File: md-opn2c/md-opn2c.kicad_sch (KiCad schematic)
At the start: 51 parts, among them U1 TL072, U3 74HCT08, U4 YM3438

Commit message: Board rev after testing initial prototype
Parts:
- removed JOUT1, JS1, JS2: Conn_01x04_Pin, Connector_JST:JST_EH_B4B-EH-A_1x04_P2.50mm_Vertical, symbol Connector:Conn_01x04_Pin
- removed JPSG1: Conn_01x02_Pin, Connector_JST:JST_EH_B2B-EH-A_1x02_P2.50mm_Vertical, symbol Connector:Conn_01x02_Pin
- removed TP_FML1, TP_FMR1: TestPoint_Small, Connector_Wire:SolderWirePad_1x01_SMD_1x2mm, symbol Connector:TestPoint_Small
- added OUT_GND1, OUT_L1, OUT_R1: TestPoint_Small, Connector_Wire:SolderWirePad_1x01_SMD_1x2mm, symbol Connector:TestPoint_Small
- R22: renamed from R24; value 10k -> 100k
- R23: renamed from R25; value 10k -> 100k
- renumbered C11 to C10, C13 to C11, C14 to C12, C15 to C13, TP_PSG1 to IN_PSG1, TP_SCDL1 to IN_SL1, TP_CRTL1 to IN_SL2, TP_SCDR1 to IN_SR1, TP_CRTR1 to IN_SR2, R8 to R10, R9 to R11, R10 to R12, R11 to R13, R16 to R14, R17 to R15, R18 to R16, R19 to R17, R20 to R18, R21 to R19, R22 to R20, R23 to R21, R12 to R8, R14 to R9, U3 to U2, U4 to U3
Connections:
- net BIAS_2_5V: now also U1.3 (+), U1.5 (+); no longer U1.2 (-), U1.6 (-)
- net GNDA: now also OUT_GND1.1
- net MIX_L: now also U1.2 (-); no longer U1.3 (+)
- net MIX_R: now also U1.6 (-); no longer U1.5 (+)
- net OUT_L: now also OUT_L1.1; no longer R22.1
- net OUT_R: now also OUT_R1.1; no longer R23.1
- net BUF_L: now reaches C9.2, R16.2, R18.1, U1.1
- net BUF_L: now also R22.1
- net BUF_R: now reaches C10.2, R17.2, R19.1, U1.7
- net BUF_R: now also R23.1
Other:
- note added: "Reduce the value of C9/C10 to increase the cutoff frequency."
- moved on the sheet: R22, R23

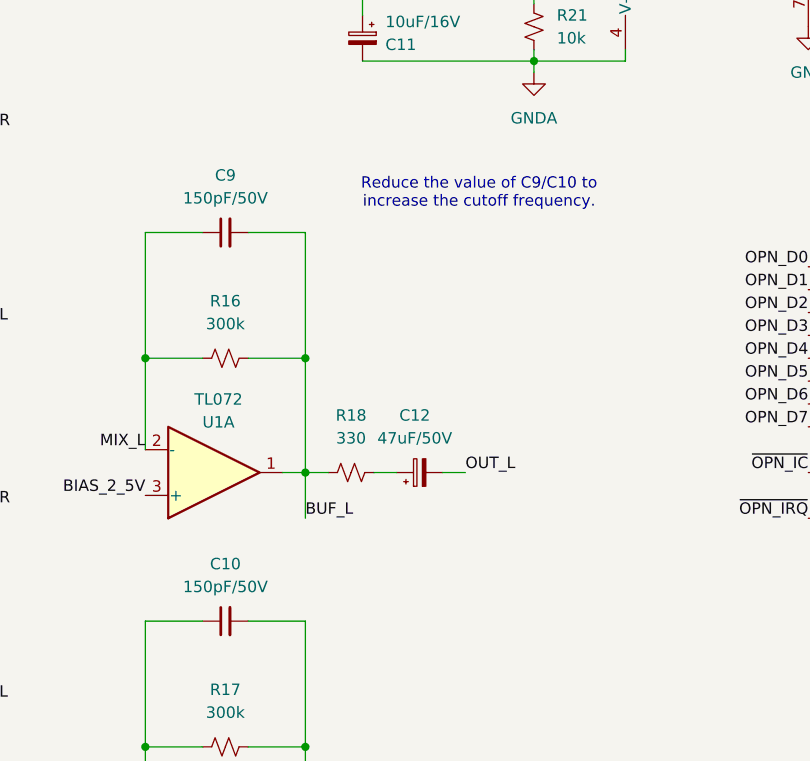
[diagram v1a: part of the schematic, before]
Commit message: Defaulted filter to ~16KHz, tidied up board
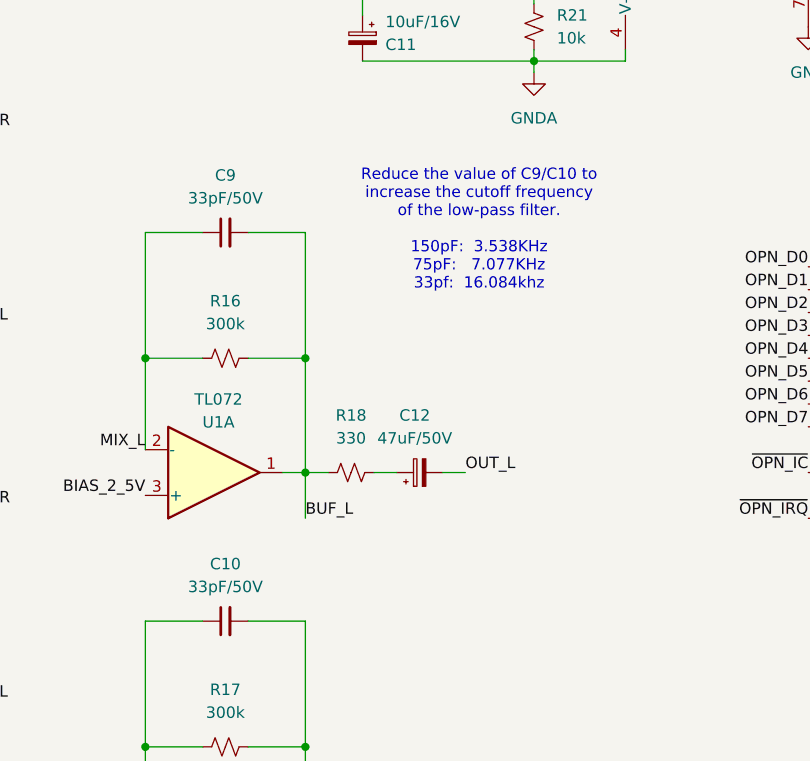
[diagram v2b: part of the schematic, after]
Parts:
- C10, C9: value 150pF/50V -> 33pF/50V
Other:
- note added: "Reduce the value of C9/C10 to increase the cutoff frequency of the low-pass filter. 150pF: 3.538KHz 75pF: 7.077KHz 33pf: 16.084khz"
- note removed: "Reduce the value of C9/C10 to increase the cutoff frequency."
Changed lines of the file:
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@@
 		)
 	)
-	(text "Reduce the value of C9/C10 to\nincrease the cutoff frequency."
+	(text "Reduce the value of C9/C10 to\nincrease the cutoff frequency\nof the low-pass filter.\n\n150pF:  3.538KHz\n75pF:   7.077KHz\n33pf:  16.084khz"
 		(exclude_from_sim no)
-		(at 146.304 70.612 0)
+		(at 146.304 74.676 0)
 		(effects
 			(font
@@
 			)
 		)
-		(property "Value" "150pF/50V"
+		(property "Value" "33pF/50V"
 			(at 118.1163 114.3 90)
 			(show_name no)
@@
 			)
 		)
-		(property "Value" "150pF/50V"
+		(property "Value" "33pF/50V"
 			(at 118.1163 71.12 90)
 			(show_name no)

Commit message: Updated readme for upcoming V1.0.1 revision
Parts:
- added JP1, JP2: SolderJumper_3_Open, Jumper:SolderJumper-3_P2.0mm_Open_TrianglePad1.0x1.5mm, symbol Jumper:SolderJumper_3_Open
- added R24, R25: 10k, Resistor_SMD:R_0603_1608Metric, symbol Device:R_Small_US
- C1, C2: footprint Capacitor_SMD:C_0805_2012Metric -> Capacitor_SMD:C_0603_1608Metric; Digikey PN (none) -> 490-10729-2-ND; PN (none) -> GRM188R61C106MAALD
- C10, C9: footprint Capacitor_SMD:C_0805_2012Metric -> Capacitor_SMD:C_0603_1608Metric; Digikey PN (none) -> 399-C0603C330K4HACTUTR-ND; PN (none) -> C0603C330K4HACTU
- C11: Digikey PN (none) -> 732-8593-1-ND; PN (none) -> 860010372001
- C12, C13: Digikey PN (none) -> 732-8823-1-ND; PN (none) -> 860020472006
- C3, C4, C5, C6, C7, C8: footprint Capacitor_SMD:C_0805_2012Metric -> Capacitor_SMD:C_0603_1608Metric; Digikey PN (none) -> 587-1241-2-ND; PN (none) -> EMK107B7105KA-T
- IN_PSG1, IN_SL1, IN_SL2, IN_SR1, IN_SR2, OUT_GND1, OUT_L1, OUT_R1: now left out of the parts list
- JOPN1: value YM2612 Socket -> DIP24 Header; Digikey PN (none) -> 1175-1524-5-ND; PN (none) -> 220-1-24-006; now in the parts list
- R10, R11, R12, R13, R14, R15: footprint Resistor_SMD:R_0805_2012Metric -> Resistor_SMD:R_0603_1608Metric; Digikey PN (none) -> 2019-RK73H1JTTD2103FTR-ND; PN (none) -> RK73H1JTTD2103F
- R16, R17: footprint Resistor_SMD:R_0805_2012Metric -> Resistor_SMD:R_0603_1608Metric; Digikey PN (none) -> 749-MCT06030D3003BP500TR-ND; PN (none) -> MCT06030D3003BP500
- R18, R19: footprint Resistor_SMD:R_0805_2012Metric -> Resistor_SMD:R_0603_1608Metric; Digikey PN (none) -> 2019-SG73P1JTTD3300FTR-ND; PN (none) -> SG73P1JTTD3300F
- R20, R21: footprint Resistor_SMD:R_0805_2012Metric -> Resistor_SMD:R_0603_1608Metric; Digikey PN (none) -> P210KHTR-ND; PN (none) -> ERJ-3EKF2103V
- R22, R23, R8, R9: footprint Resistor_SMD:R_0805_2012Metric -> Resistor_SMD:R_0603_1608Metric; Digikey PN (none) -> 2019-RK73H1JTTD1003FTR-ND; PN (none) -> RK73H1JTTD1003F
- U1: value TL072 -> TL972; Digikey PN (none) -> 296-22842-2-ND; PN (none) -> TL972IDR
- U2: Digikey PN (none) -> 296-14862-2-ND; PN (none) -> SN74HCT08DR
- U3: now not fitted; now left out of the parts list
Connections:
- net MIX_L: now also JP1.2 (C); no longer R8.2
- net MIX_R: now also JP2.2 (C); no longer R9.2
- net at C1.2, R8.1: now also R24.2
- net at C2.2, R9.1: now also R25.2
- new net: JP1.1 (A), R24.1
- new net: JP1.3 (B), R8.2
- new net: JP2.1 (A), R25.1
- new net: JP2.3 (B), R9.2
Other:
- moved on the sheet: R8, R9

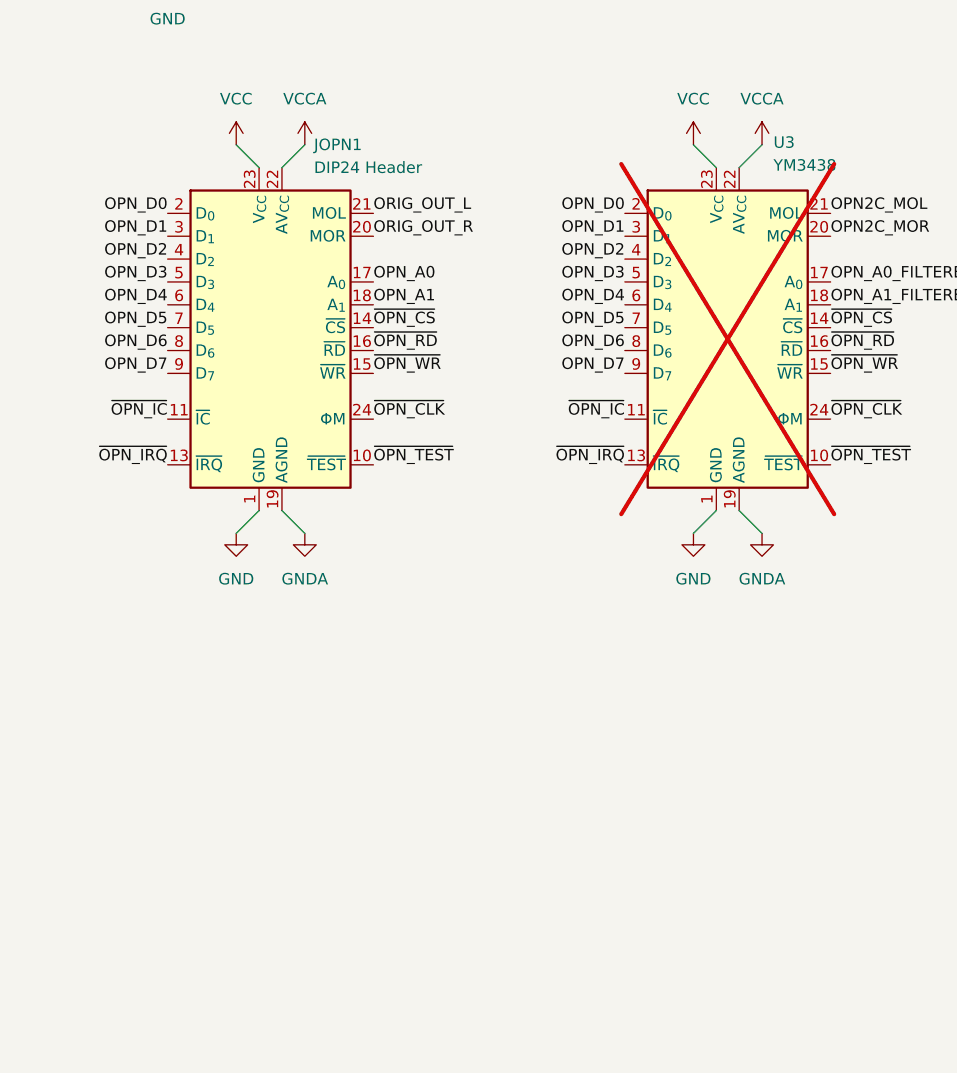
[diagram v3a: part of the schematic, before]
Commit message: Reduced BOM cost by a few bucks
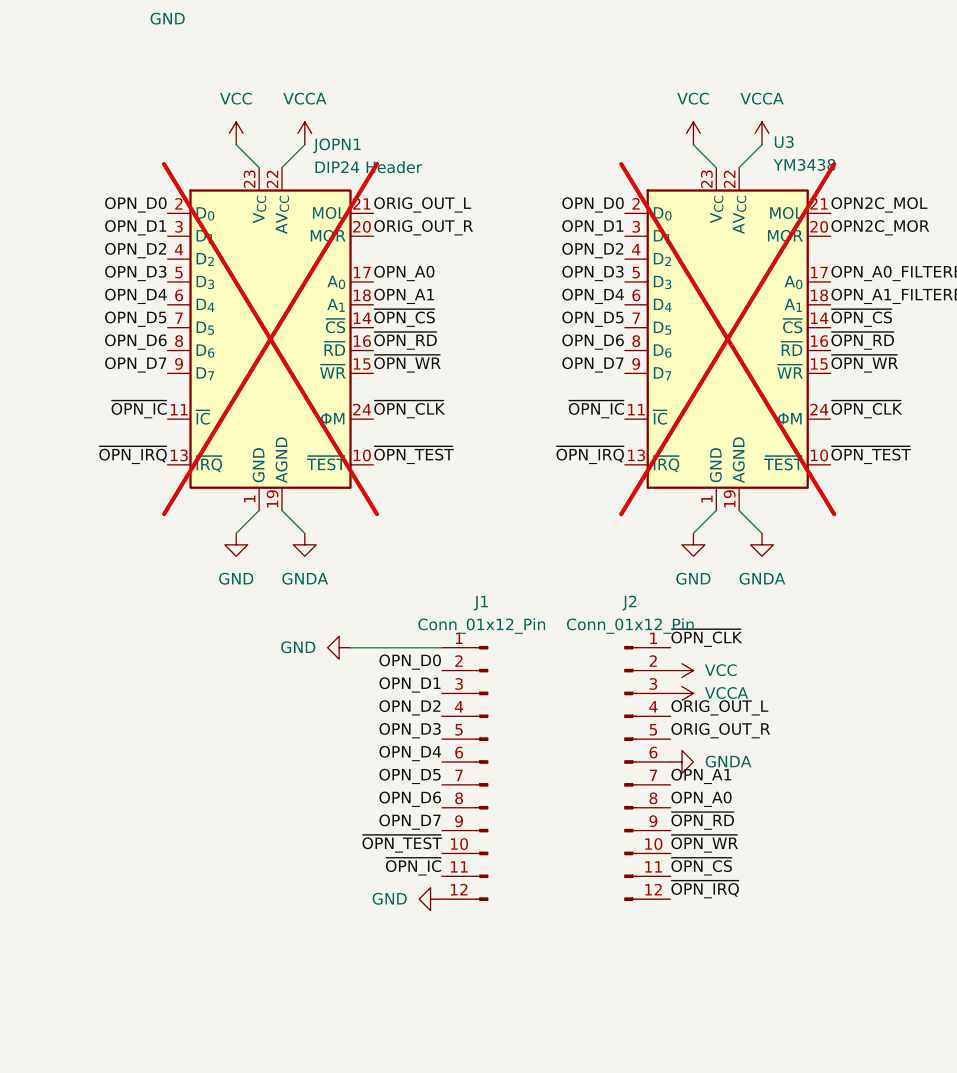
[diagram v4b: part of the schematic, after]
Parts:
- added J1, J2: Conn_01x12_Pin, Connector_PinHeader_2.54mm:PinHeader_1x12_P2.54mm_Vertical, symbol Connector:Conn_01x12_Pin
- JOPN1: now not fitted; now left out of the parts list
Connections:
- net GND: now also J1.1 (Pin_1), J1.12 (Pin_12)
- net GNDA: now also J2.6 (Pin_6)
- net OPN_A0: now also J2.8 (Pin_8)
- net OPN_A1: now also J2.7 (Pin_7)
- net OPN_D0: now also J1.2 (Pin_2)
- net OPN_D1: now also J1.3 (Pin_3)
- net OPN_D2: now also J1.4 (Pin_4)
- net OPN_D3: now also J1.5 (Pin_5)
- net OPN_D4: now also J1.6 (Pin_6)
- net OPN_D5: now also J1.7 (Pin_7)
- net OPN_D6: now also J1.8 (Pin_8)
- net OPN_D7: now also J1.9 (Pin_9)
- net ORIG_OUT_L: now also J2.4 (Pin_4)
- net ORIG_OUT_R: now also J2.5 (Pin_5)
- net VCC: now also J2.2 (Pin_2)
- net VCCA: now also J2.3 (Pin_3)
- net ~{OPN_CLK}: now also J2.1 (Pin_1)
- net ~{OPN_CS}: now also J2.11 (Pin_11)
- net ~{OPN_IC}: now also J1.11 (Pin_11)
- net ~{OPN_IRQ}: now also J2.12 (Pin_12)
- net ~{OPN_RD}: now also J2.9 (Pin_9)
- net ~{OPN_TEST}: now also J1.10 (Pin_10)
- net ~{OPN_WR}: now also J2.10 (Pin_10)

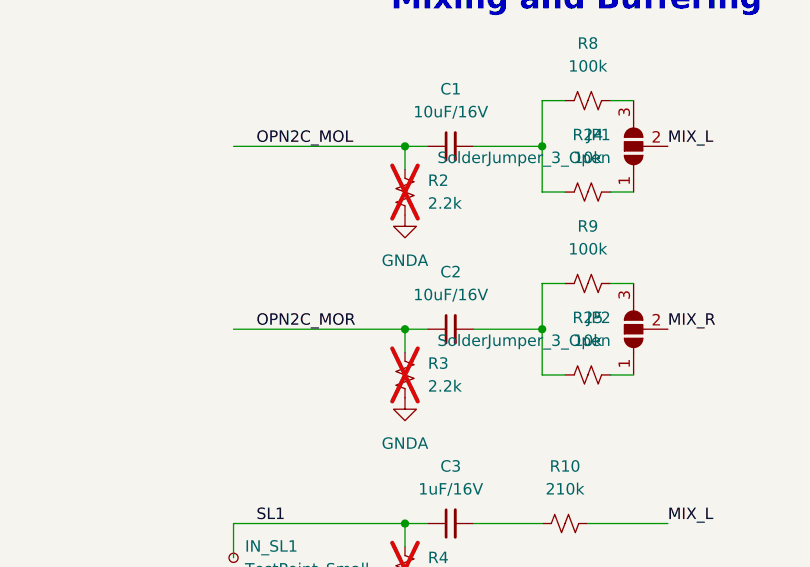
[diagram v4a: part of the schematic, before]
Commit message: 2.2k pulldowns for YM2612 implemented as optional pads on the underside; note written in README
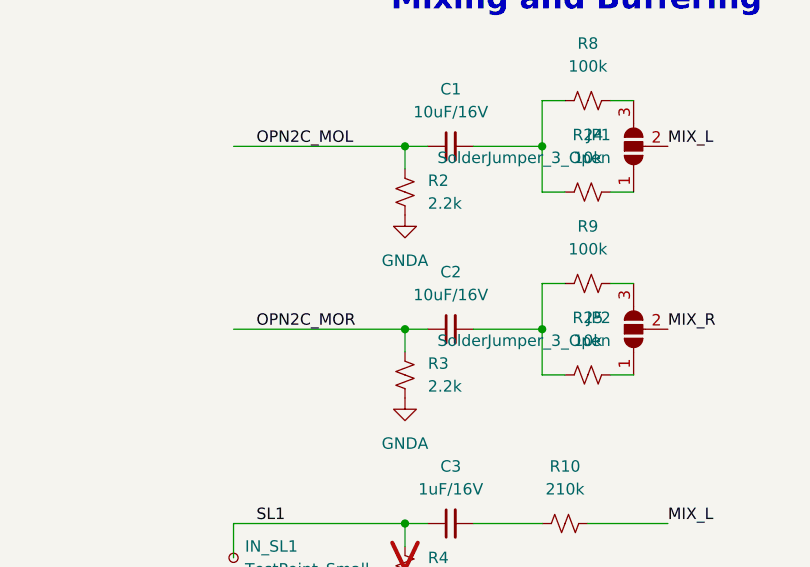
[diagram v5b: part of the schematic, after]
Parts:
- R2, R3: now fitted
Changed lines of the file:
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@@
 		(exclude_from_sim no)
 		(in_bom no)
-		(on_board no)
+		(on_board yes)
 		(in_pos_files no)
-		(dnp yes)
+		(dnp no)
 		(fields_autoplaced yes)
 		(property "Reference" "R2"
@@
 		(exclude_from_sim no)
 		(in_bom no)
-		(on_board no)
+		(on_board yes)
 		(in_pos_files no)
-		(dnp yes)
+		(dnp no)
 		(fields_autoplaced yes)
 		(property "Reference" "R3"

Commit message: v1.0.2
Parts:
- added JP3, JP4: SolderJumper_2_Open, Jumper:SolderJumper-2_P1.3mm_Open_TrianglePad1.0x1.5mm, symbol Jumper:SolderJumper_2_Open
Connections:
- net OPN2C_MOL: now also JP3.2 (B); no longer R2.1
- net OPN2C_MOR: now also JP4.2 (B); no longer R3.1
- new net: JP3.1 (A), R2.1
- new net: JP4.1 (A), R3.1
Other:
- moved on the sheet: R2, R3
